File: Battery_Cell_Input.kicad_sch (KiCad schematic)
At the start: 37 parts, among them J801 HEATER_CONN, J802 HEATER_CONN, Q801 NMOS, Q802 NMOS, U801 BQ76920PW

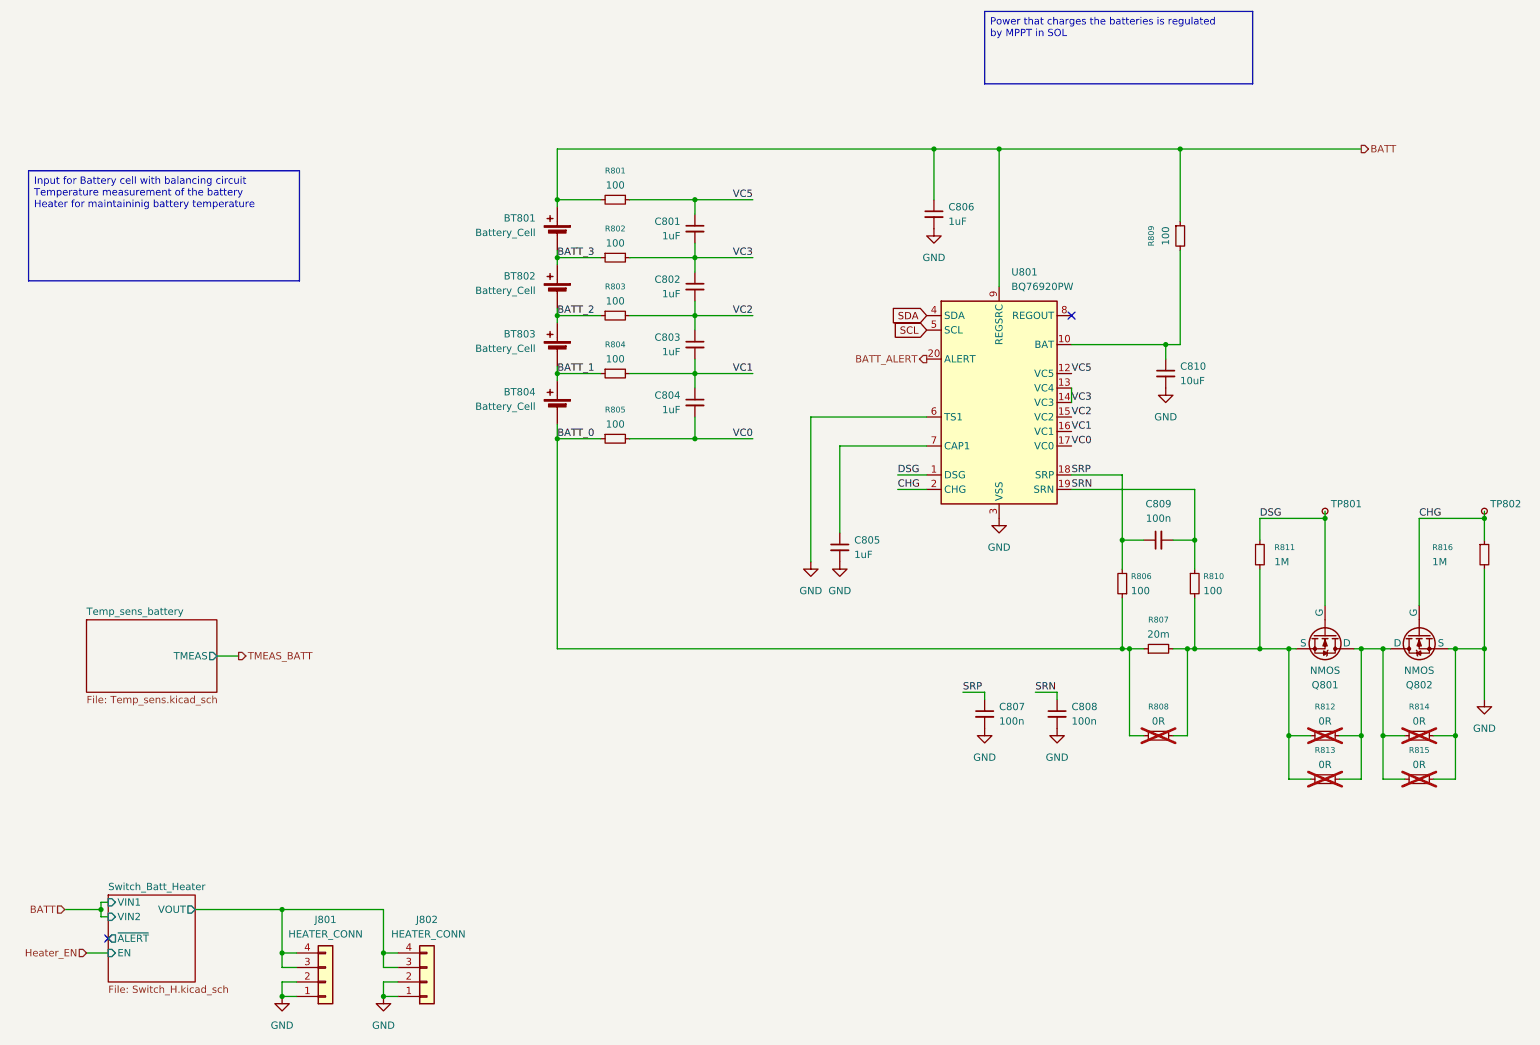
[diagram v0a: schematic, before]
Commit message: reduced number of DCDC converter for PV panels; updated test pcb
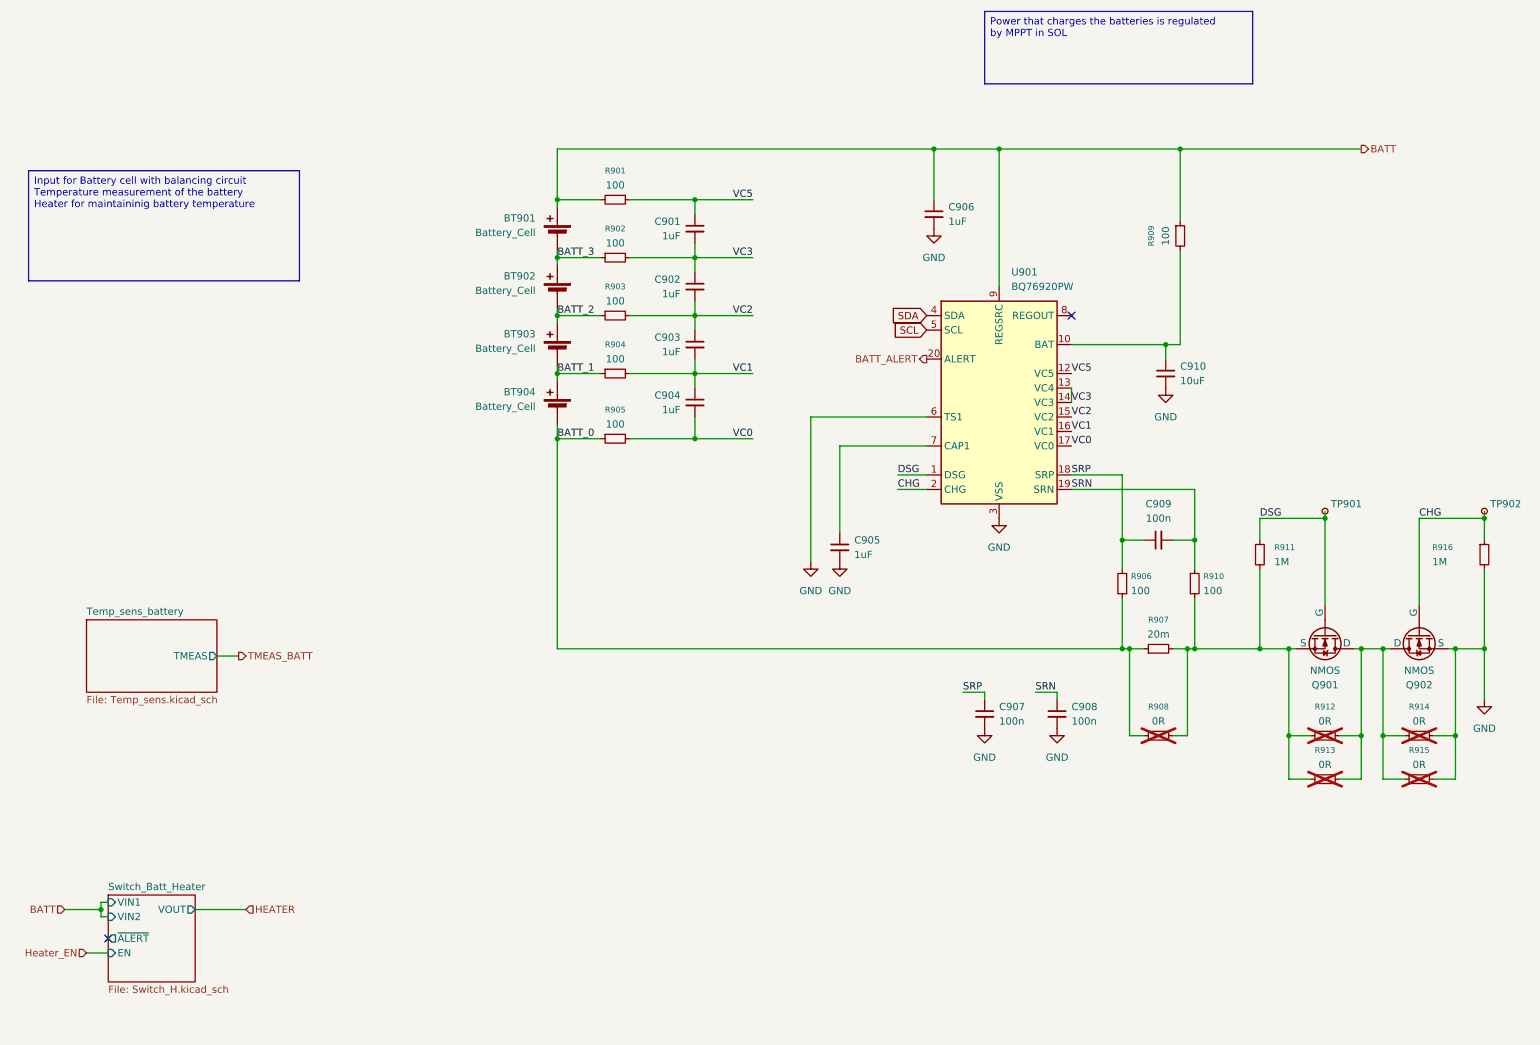
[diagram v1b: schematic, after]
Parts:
- removed J801, J802: HEATER_CONN, Connector_Molex:Molex_CLIK-Mate_505405-0470_1x04-1MP_P1.50mm_Vertical, symbol Connector_Generic:Conn_01x04
- renumbered BT801 to BT901, BT802 to BT902, BT803 to BT903, BT804 to BT904, C801 to C901, C802 to C902, C803 to C903, C804 to C904, C805 to C905, C806 to C906, C807 to C907, C808 to C908, C809 to C909, C810 to C910, Q801 to Q901, Q802 to Q902, R801 to R901, R802 to R902, R803 to R903, R804 to R904, R805 to R905, R806 to R906, R807 to R907, R808 to R908, R809 to R909, R810 to R910, R811 to R911, R812 to R912, R813 to R913, R814 to R914, R815 to R915, R816 to R916, TP801 to TP901, TP802 to TP902, U801 to U901

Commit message: added missing heater connectors
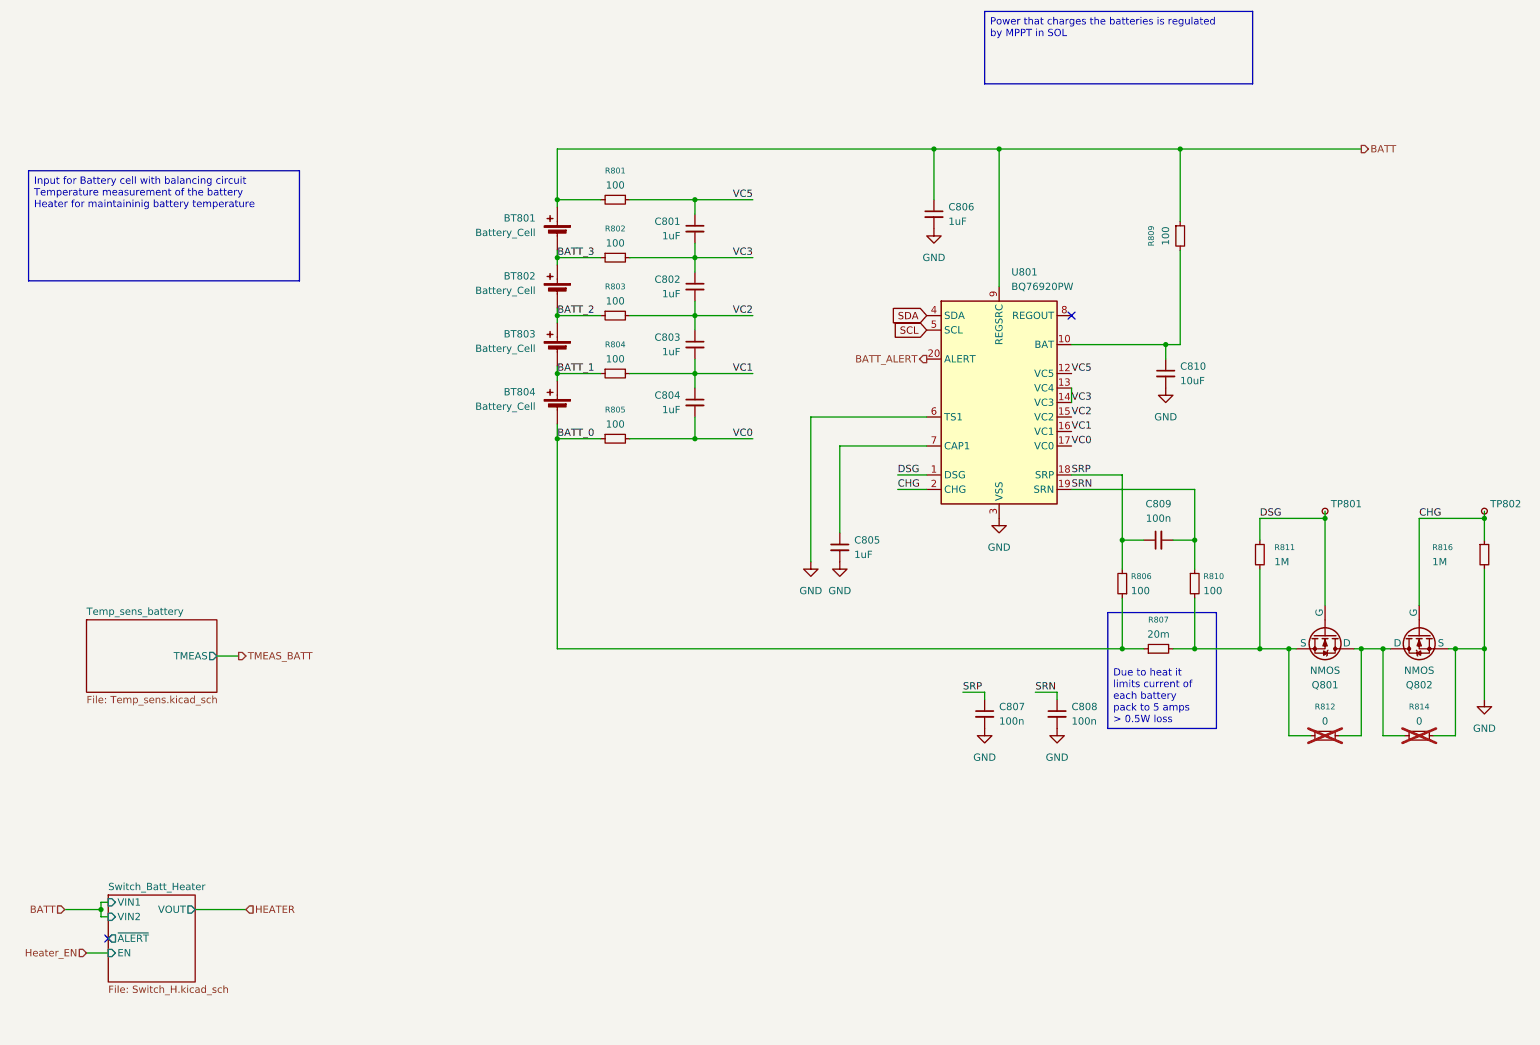
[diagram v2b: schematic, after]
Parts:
- removed R908, R913, R915: 0R, Resistor_SMD:R_0603_1608Metric_Pad0.98x0.95mm_HandSolder, symbol Device:R_Small
- R807: renamed from R907; footprint Resistor_SMD:R_0603_1608Metric_Pad0.98x0.95mm_HandSolder -> Resistor_SMD:R_1210_3225Metric_Pad1.30x2.65mm_HandSolder
- R812: renamed from R912; value 0R -> 0; footprint Resistor_SMD:R_0603_1608Metric_Pad0.98x0.95mm_HandSolder -> Resistor_SMD:R_1210_3225Metric_Pad1.30x2.65mm_HandSolder
- R814: renamed from R914; value 0R -> 0; footprint Resistor_SMD:R_0603_1608Metric_Pad0.98x0.95mm_HandSolder -> Resistor_SMD:R_1210_3225Metric_Pad1.30x2.65mm_HandSolder
- renumbered BT901 to BT801, BT902 to BT802, BT903 to BT803, BT904 to BT804, C901 to C801, C902 to C802, C903 to C803, C904 to C804, C905 to C805, C906 to C806, C907 to C807, C908 to C808, C909 to C809, C910 to C810, Q901 to Q801, Q902 to Q802, R901 to R801, R902 to R802, R903 to R803, R904 to R804, R905 to R805, R906 to R806, R909 to R809, R910 to R810, R911 to R811, R916 to R816, TP901 to TP801, TP902 to TP802, U901 to U801

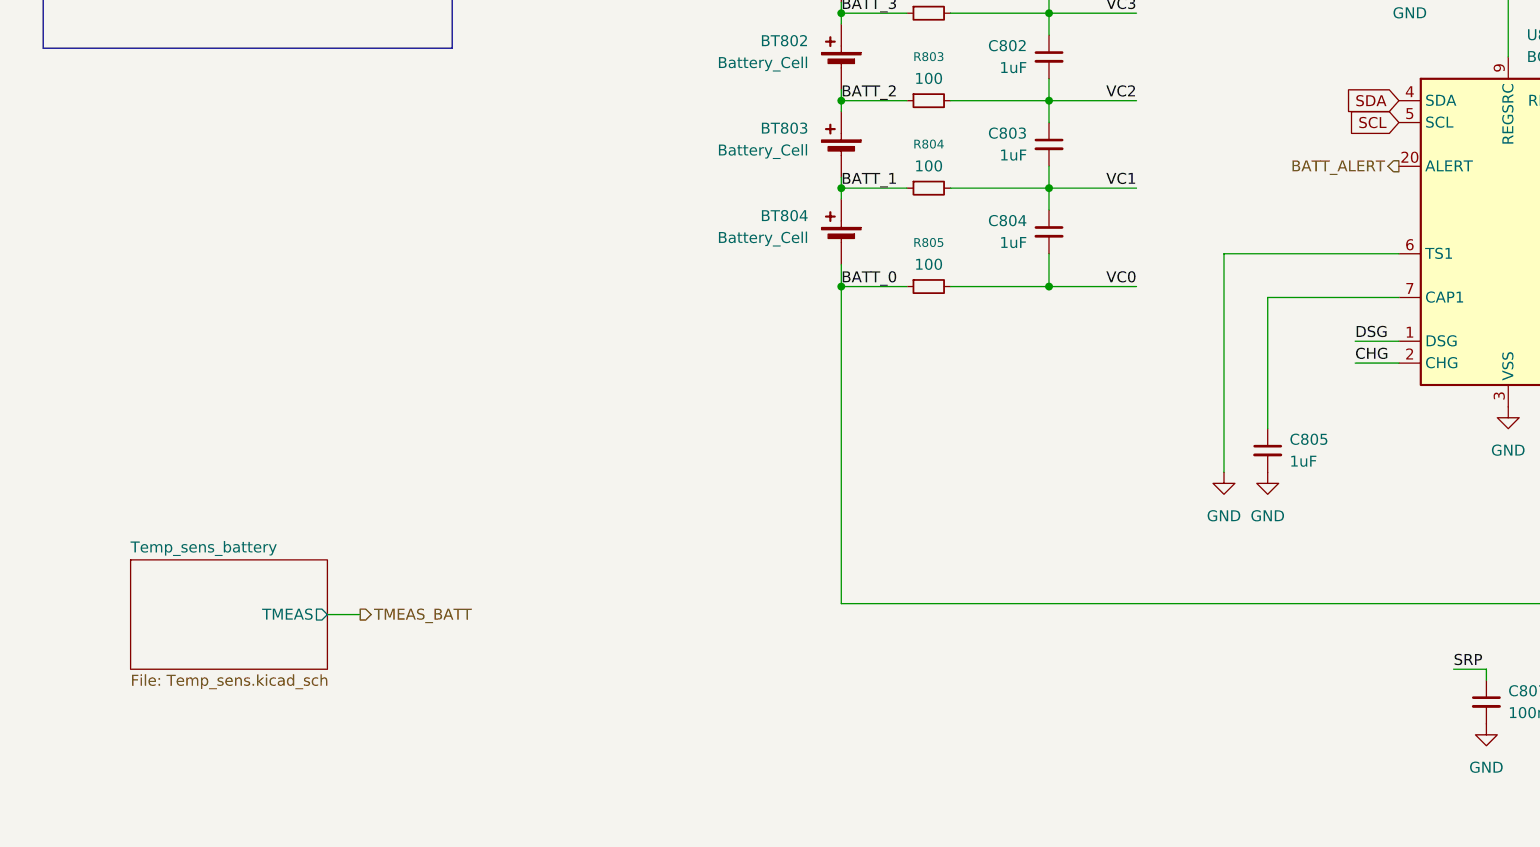
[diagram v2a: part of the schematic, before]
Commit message: replaced individual CC sourses for SOL with a single one
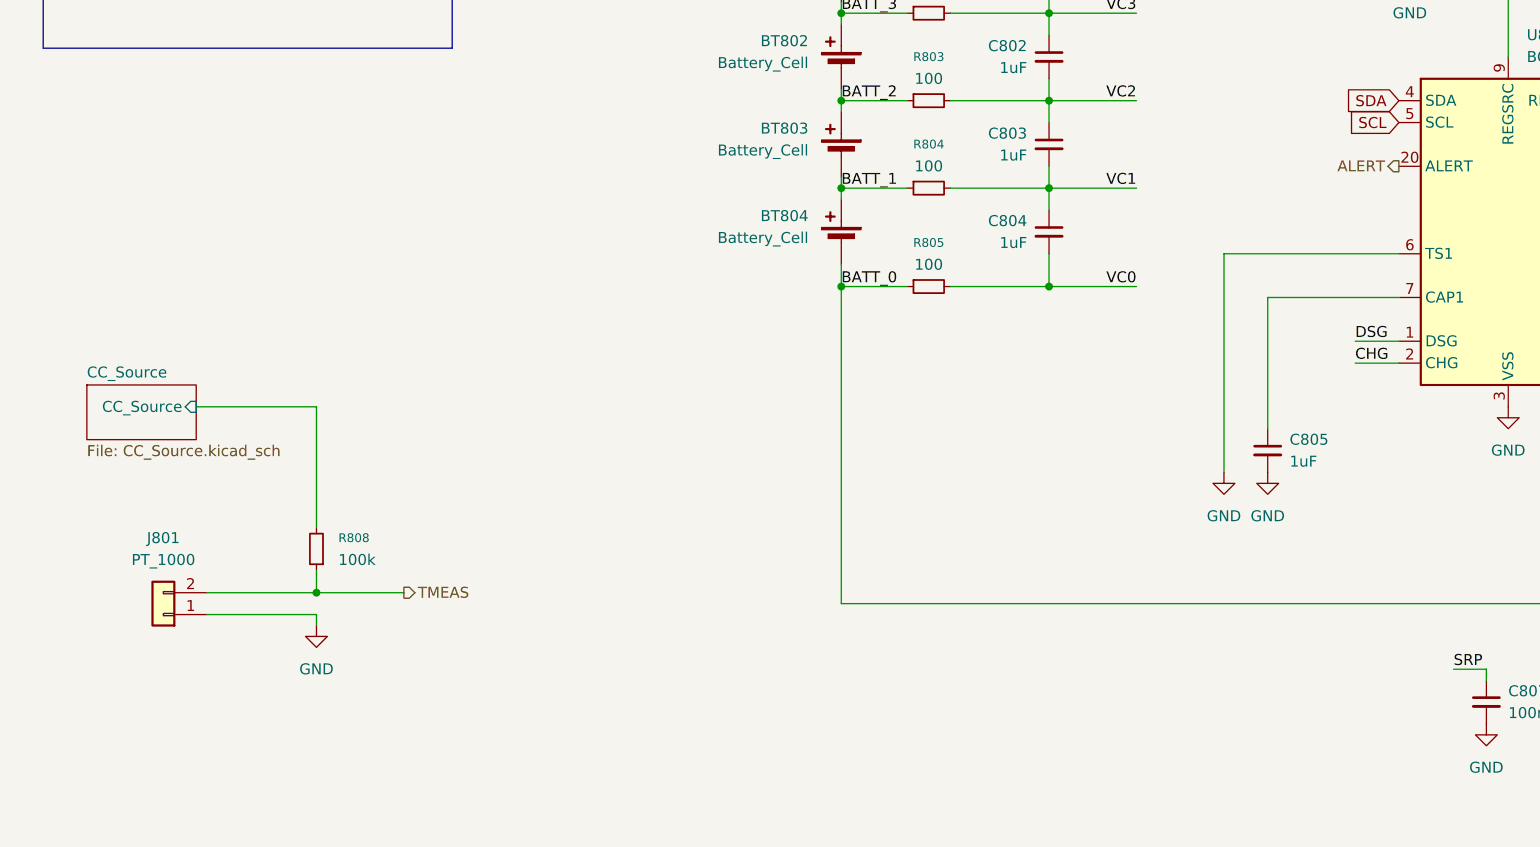
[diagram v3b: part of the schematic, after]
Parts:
- added J801: PT_1000, Connector_PinSocket_2.54mm:PinSocket_1x02_P2.54mm_Vertical, symbol Connector_Generic:Conn_01x02
- added R808: 100k, Resistor_SMD:R_0603_1608Metric_Pad0.98x0.95mm_HandSolder, symbol Device:R_Small
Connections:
- net GND: now also J801.1 (Pin_1)
- net BATT_ALERT renamed ALERT
- new net CC_Source/CC_Source: R808.2
- new net TMEAS: J801.2 (Pin_2), R808.1
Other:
- removed sheet Temp_sens_battery
- added sheet CC_Source (CC_Source.kicad_sch)
